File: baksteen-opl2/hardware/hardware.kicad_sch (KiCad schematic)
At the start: 48 parts, among them J1 AudioJack2, J2 AudioJack2, J3 AudioJack2, J4 AudioJack2, J5 AudioJack2, J6 AudioJack2, J7 AudioJack2, J8 AudioJack2, J9 AudioJack2, SW1 Encoder, SW2 SW_Push, SW3 SW_Push

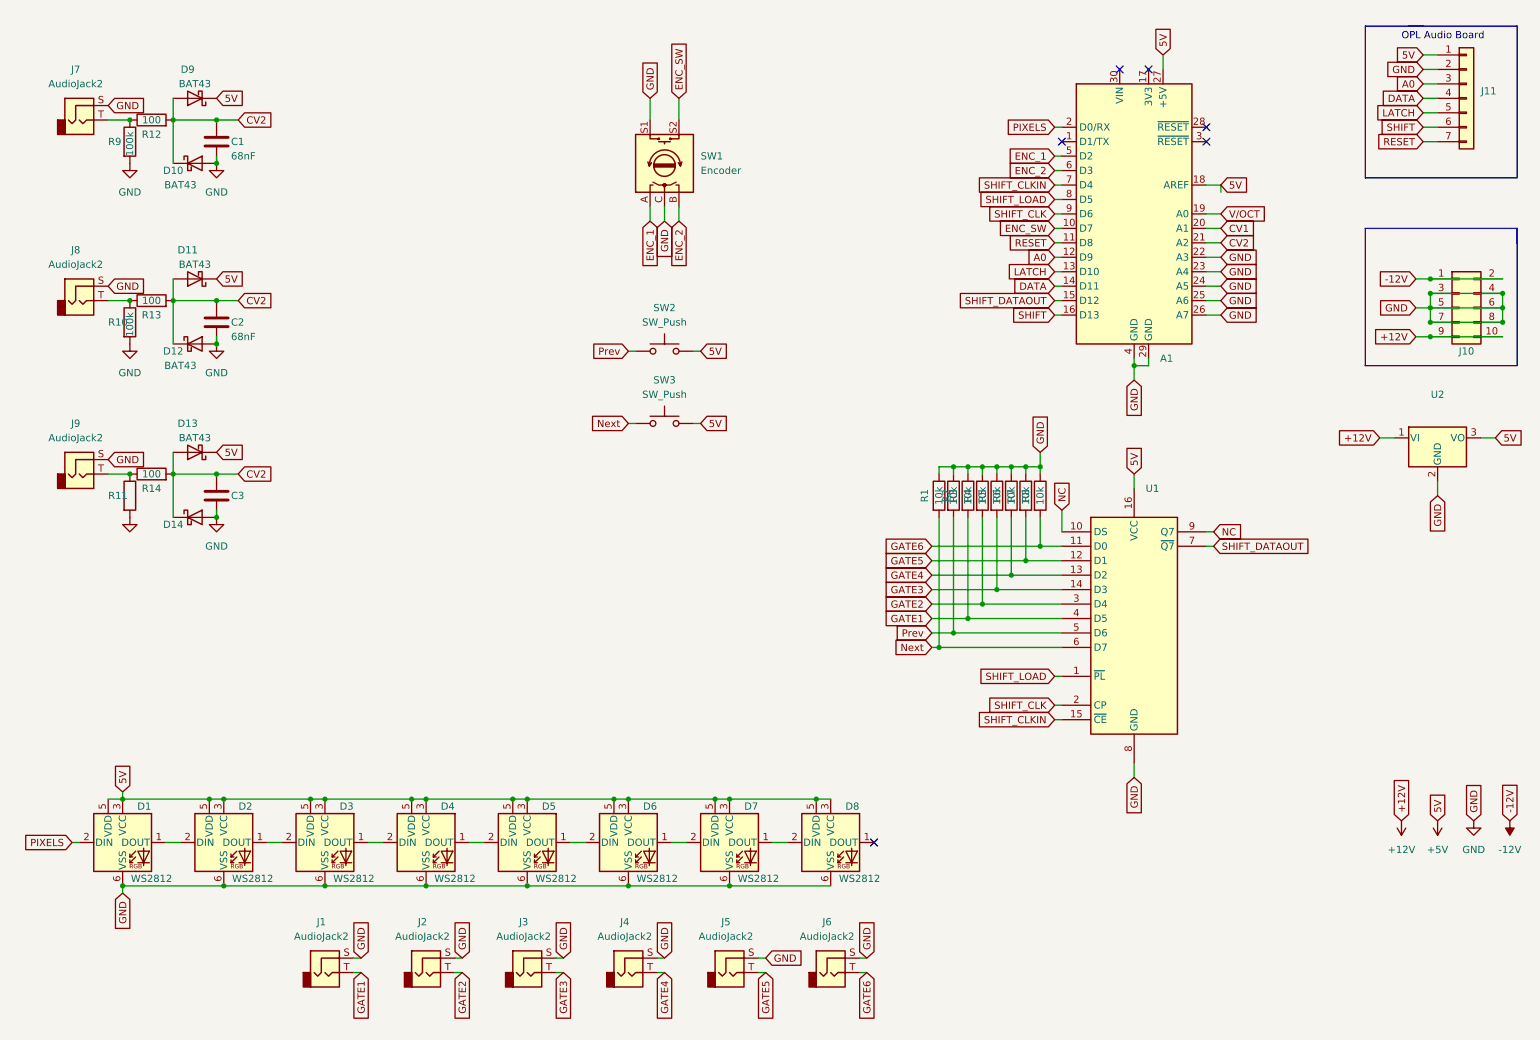
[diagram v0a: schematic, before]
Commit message: removed nano, going with bare atmega328p in tqfp package
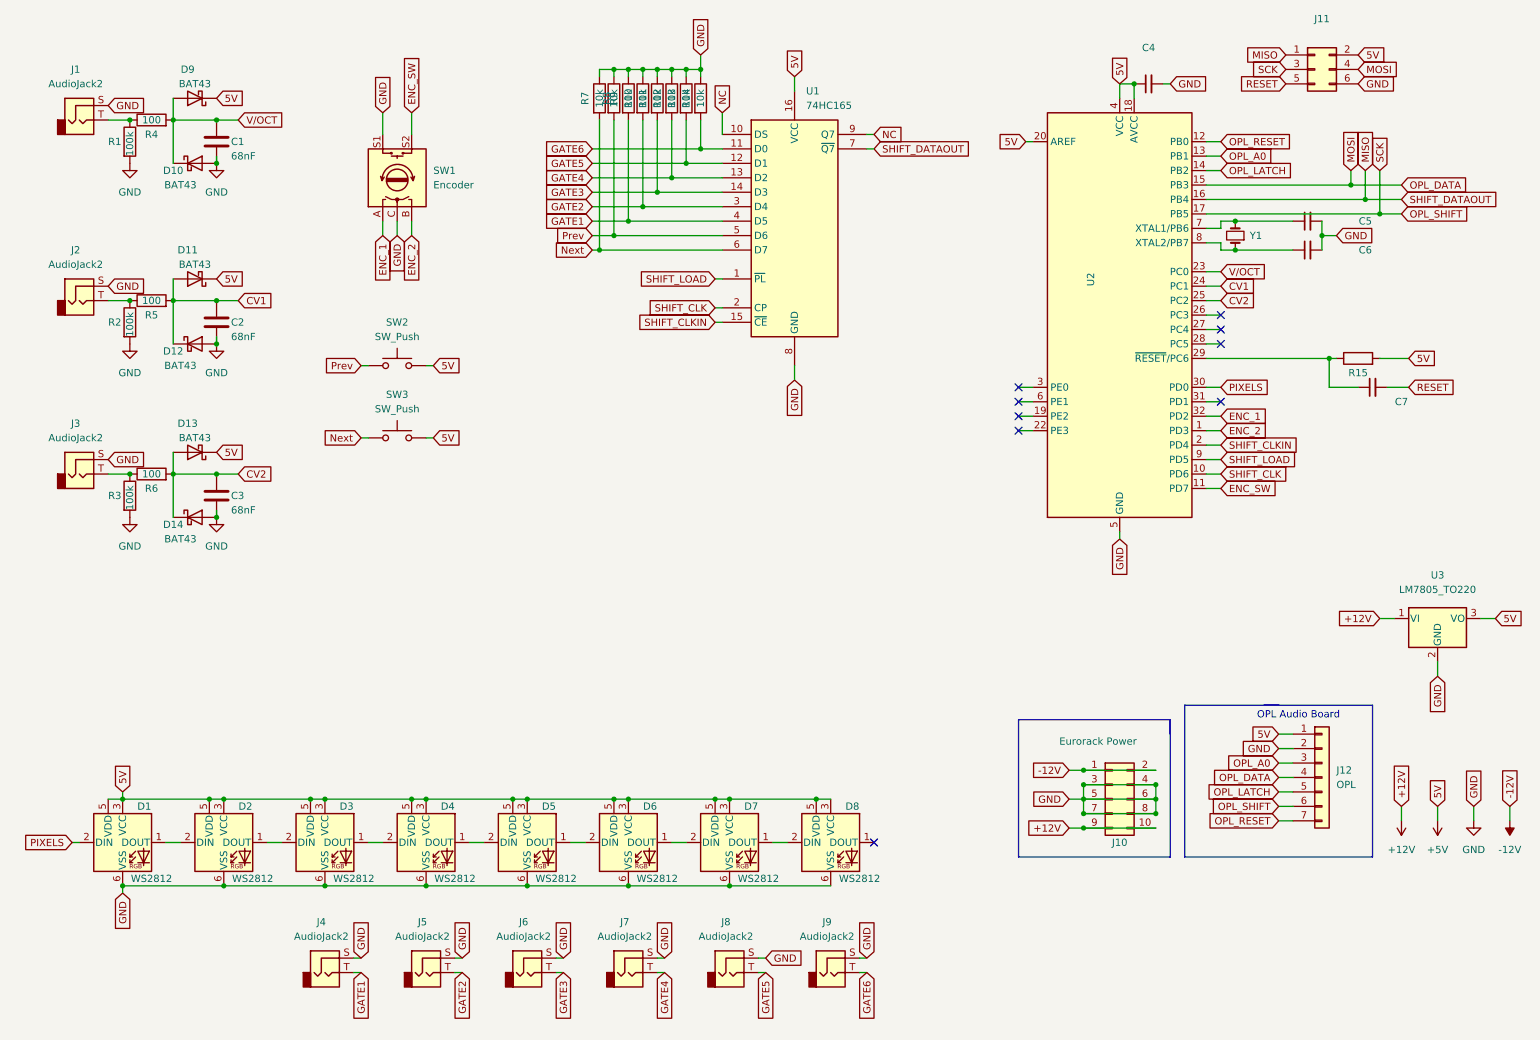
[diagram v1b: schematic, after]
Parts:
- removed A1: (no value), symbol MCU_Module:Arduino_Nano_v3.x
- added C4, C5, C6, C7: (no value), symbol Device:C_Small
- added J11: (no value), symbol Connector_Generic:Conn_02x03_Odd_Even
- added R15: (no value), symbol Device:R
- added U2: (no value), symbol MCU_Microchip_ATmega:ATmega328PB-A
- added Y1: (no value), symbol Device:Crystal_Small
- C1, C2: footprint (none) -> Capacitor_SMD:C_0805_2012Metric
- C3: value (none) -> 68nF; footprint (none) -> Capacitor_SMD:C_0805_2012Metric
- D10, D11, D12, D13, D9: footprint (none) -> Diode_SMD:D_0805_2012Metric
- D14: value (none) -> BAT43; footprint (none) -> Diode_SMD:D_0805_2012Metric
- J10: value (none) -> Eurorack Power; footprint (none) -> Connector_IDC:IDC-Header_2x05_P2.54mm_Vertical
- J12: renamed from J11; value (none) -> OPL; footprint (none) -> Connector_PinSocket_2.54mm:PinSocket_1x07_P2.54mm_Vertical
- R1: renamed from R9; footprint (none) -> Resistor_SMD:R_0805_2012Metric
- R10: renamed from R4; footprint (none) -> Resistor_SMD:R_0805_2012Metric
- R11: renamed from R5; footprint (none) -> Resistor_SMD:R_0805_2012Metric
- R12: renamed from R6; footprint (none) -> Resistor_SMD:R_0805_2012Metric
- R13: renamed from R7; footprint (none) -> Resistor_SMD:R_0805_2012Metric
- R14: renamed from R8; footprint (none) -> Resistor_SMD:R_0805_2012Metric
- R2: renamed from R10; footprint (none) -> Resistor_SMD:R_0805_2012Metric
- R3: renamed from R11; value (none) -> 100k; footprint (none) -> Resistor_SMD:R_0805_2012Metric
- R4: renamed from R12; footprint (none) -> Resistor_SMD:R_0805_2012Metric
- R5: renamed from R13; footprint (none) -> Resistor_SMD:R_0805_2012Metric
- R6: renamed from R14; footprint (none) -> Resistor_SMD:R_0805_2012Metric
- R7: renamed from R1; footprint (none) -> Resistor_SMD:R_0805_2012Metric
- R8: renamed from R2; footprint (none) -> Resistor_SMD:R_0805_2012Metric
- R9: renamed from R3; footprint (none) -> Resistor_SMD:R_0805_2012Metric
- U1: value (none) -> 74HC165; footprint (none) -> Package_SO:SOIC-16_3.9x9.9mm_P1.27mm
- U3: renamed from U2; value (none) -> LM7805_TO220; footprint (none) -> Package_TO_SOT_SMD:SOT-223-3_TabPin2
- renumbered J7 to J1, J8 to J2, J9 to J3, J1 to J4, J2 to J5, J3 to J6, J4 to J7, J5 to J8, J6 to J9
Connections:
- net +5V: now also C4.1, J11.2 (Pin_2), R15.2, U2.18 (AVCC), U2.20 (AREF), U2.4 (VCC)
- net CV1: now also C2.1, D11.2 (A), D12.1 (K), R5.2, U2.24 (PC1)
- net CV2: now also U2.25 (PC2); no longer C1.1, C2.1, D10.1 (K), D11.2 (A), D12.1 (K), D9.2 (A), R4.2, R5.2
- net ENC_1: now also U2.32 (PD2)
- net ENC_2: now also U2.1 (PD3)
- net ENC_SW: now also U2.11 (PD7)
- net GND: now also C4.2, C5.2, C6.2, J11.6 (Pin_6), U2.21 (GND), U2.5 (GND)
- net PIXELS: now also U2.30 (PD0)
- net RESET: now also C7.2, J11.5 (Pin_5); no longer J12.7 (Pin_7)
- net SHIFT_CLK: now also U2.10 (PD6)
- net SHIFT_CLKIN: now also U2.2 (PD4)
- net SHIFT_LOAD: now also U2.9 (PD5)
- net V/OCT: now also C1.1, D10.1 (K), D9.2 (A), R4.2, U2.23 (PC0)
- net A0 renamed OPL_A0
- net OPL_A0: now also U2.13 (PB1)
- net DATA renamed MOSI
- net MOSI: now also J11.4 (Pin_4), U2.15 (PB3)
- net LATCH renamed OPL_LATCH
- net OPL_LATCH: now also U2.14 (PB2)
- net SHIFT renamed OPL_SHIFT
- net OPL_SHIFT: now also J11.3 (Pin_3), U2.17 (PB5)
- net SHIFT_DATAOUT renamed MISO
- net MISO: now also J11.1 (Pin_1), U2.16 (PB4)
- new net: C7.1, R15.1, U2.29 (~{RESET}/PC6)
- new net: C5.1, U2.7 (XTAL1/PB6), Y1.2
- new net: C6.1, U2.8 (XTAL2/PB7), Y1.1
- new net OPL_RESET: J12.7 (Pin_7), U2.12 (PB0)
- no-connect marks 6 -> 9
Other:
- company: (none) -> David Higgins
- title: (none) -> OPL Eurorack Module
- moved on the sheet: J10, J12, R10, R11, R12, R13, R14, R7, R8, R9, SW1, SW2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

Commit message: added tracks ... mostly
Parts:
- J1, J2, J3, J4, J5, J6, J7, J8, J9: value AudioJack2 -> (none)
- J12: value OPL -> (none); footprint Connector_PinSocket_2.54mm:PinSocket_1x07_P2.54mm_Vertical -> (none)
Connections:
- net GND: now also J1.T, J2.T, J3.T, R1.1, R2.1, R3.1, R4.1, R5.1, R6.1; no longer J1.S, J2.S, J3.S

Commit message: reran tracks ... mostly complete, couple DRC errors
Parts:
- J1, J2, J4, J5, J6, J7, J8, J9: symbol Connector:AudioJack2 -> Connector:AudioJack2_SwitchT
- J3: footprint Connector_Audio:Jack_3.5mm_QingPu_WQP-PJ398SM_Vertical_CircularHoles -> (none); symbol Connector:AudioJack2 -> Connector:AudioJack2_SwitchT
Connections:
- net GND: now also J1.S, J2.S, J3.S; no longer J1.T, J2.T, J3.T, R1.1, R2.1, R3.1, R4.1, R5.1, R6.1
- net NC: no longer names the net of U1.10 (DS)
- net NC: no longer U1.9 (Q7)
- new net: J3.T, R3.1, R6.1
- new net: J2.T, R2.1, R5.1
- new net: J1.T, R1.1, R4.1
- no-connect marks 9 -> 20
